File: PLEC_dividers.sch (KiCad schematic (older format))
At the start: 24 parts

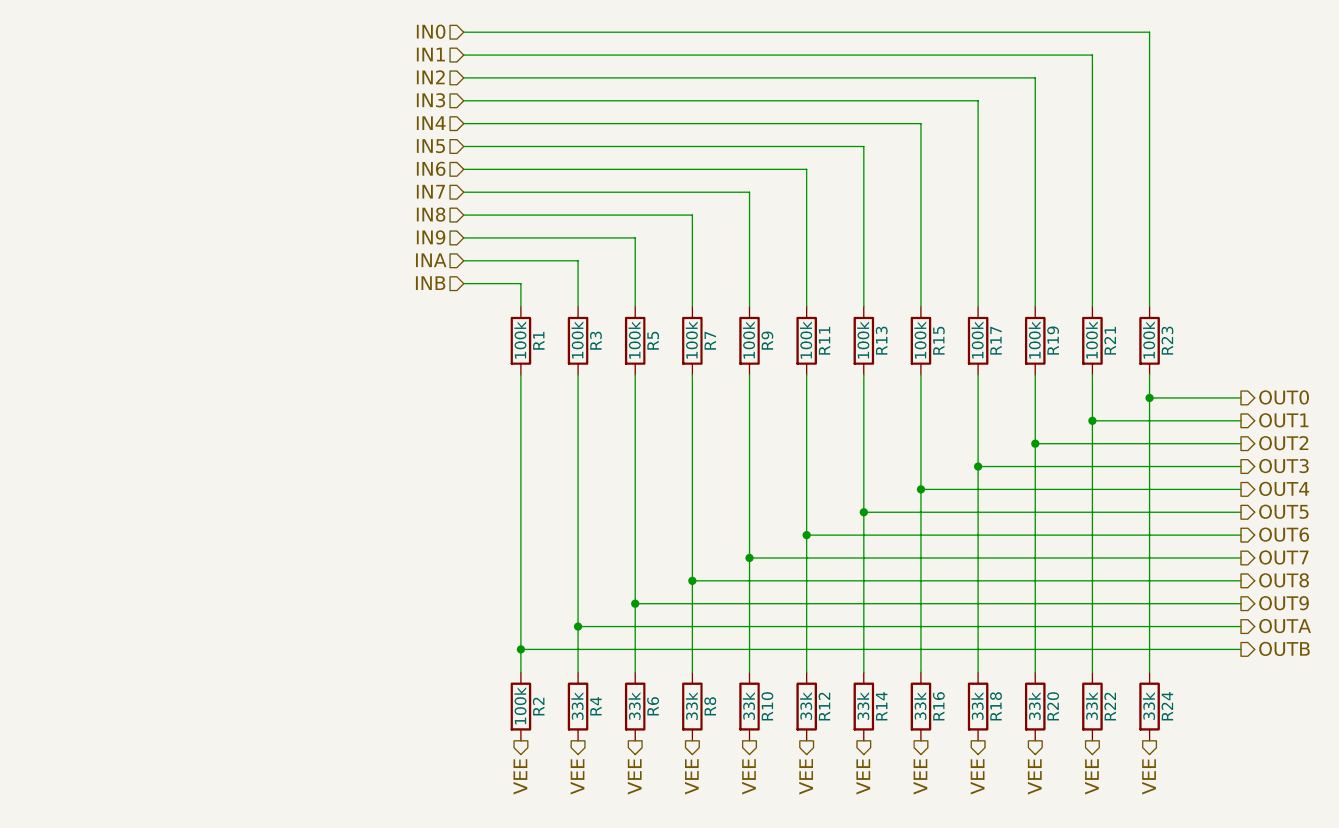
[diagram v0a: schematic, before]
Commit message: Replaced solid state relays with NPN Darlingtons
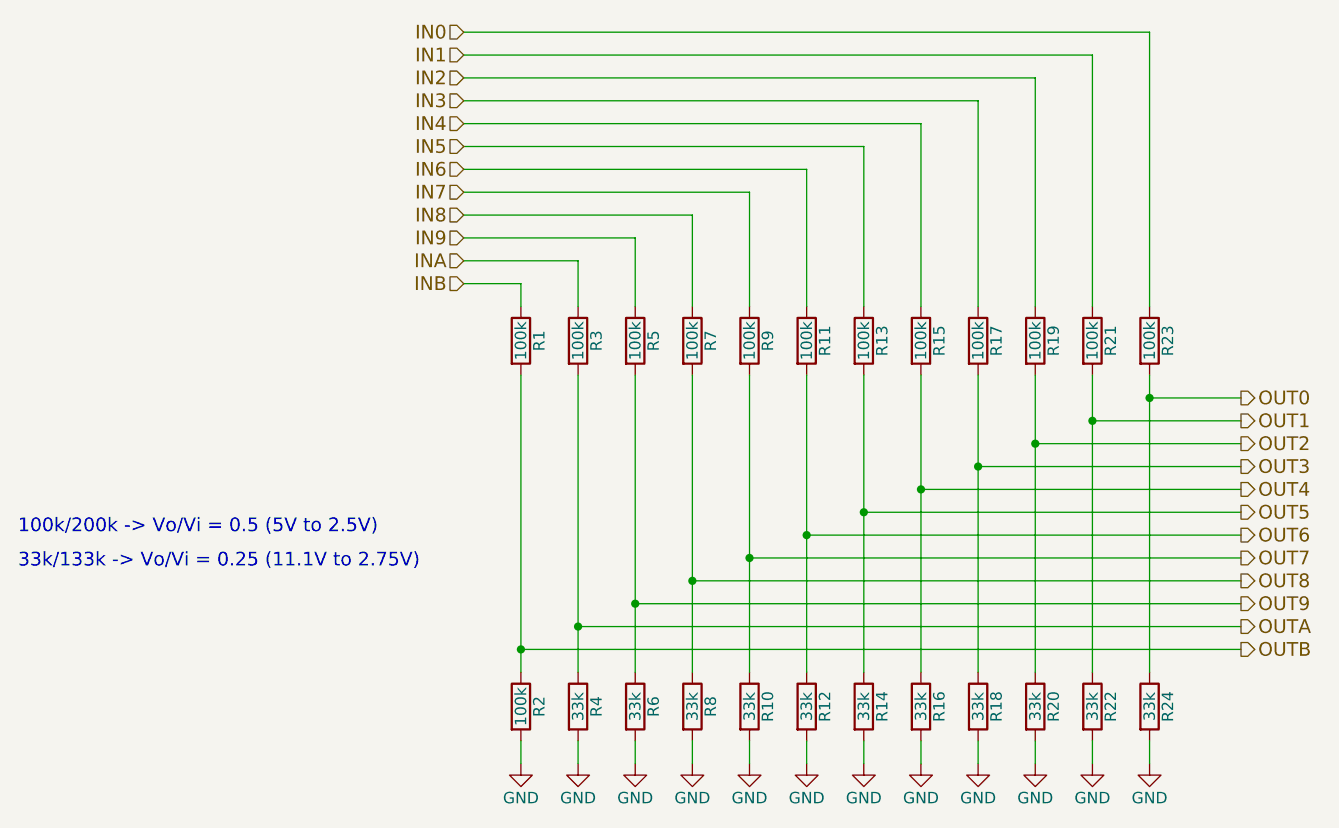
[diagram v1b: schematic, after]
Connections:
- net VEE renamed GND
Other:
- note added: "100k/200k -> Vo/Vi = 0.5 (5V to 2.5V)"
- note added: "33k/133k -> Vo/Vi = 0.25 (11.1V to 2.75V)"
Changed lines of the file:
@@
 EESchema Schematic File Version 2
+LIBS:PLEC-rescue
 LIBS:power
 LIBS:device
@@
 LIBS:PLEC
 LIBS:cap_470u
+LIBS:BDW42G
 LIBS:PLEC-cache
 EELAYER 25 0
@@
 Text HLabel 7400 4300 2    60   Output ~ 0
 OUT9
-Text HLabel 4750 4900 3    60   Output ~ 0
-VEE
-Text HLabel 5000 4900 3    60   Output ~ 0
-VEE
-Text HLabel 5250 4900 3    60   Output ~ 0
-VEE
-Text HLabel 5500 4900 3    60   Output ~ 0
-VEE
-Text HLabel 5750 4900 3    60   Output ~ 0
-VEE
-Text HLabel 6000 4900 3    60   Output ~ 0
-VEE
-Text HLabel 6250 4900 3    60   Output ~ 0
-VEE
-Text HLabel 6500 4900 3    60   Output ~ 0
-VEE
-Text HLabel 6750 4900 3    60   Output ~ 0
-VEE
-Text HLabel 7000 4900 3    60   Output ~ 0
-VEE
 $Comp
 L R R3
@@
 Text HLabel 4000 2800 0    60   Input ~ 0
 INA
-Text HLabel 4500 4900 3    60   Output ~ 0
-VEE
 Wire Wire Line
 	7400 4300 4750 4300
@@
 	1    0    0    -1
 $EndComp
-Text HLabel 4250 4900 3    60   Output ~ 0
-VEE
 Wire Wire Line
 	4250 3300 4250 4600
@@
 Text HLabel 7400 4500 2    60   Output ~ 0
 OUTB
+$Comp
+L GND #PWR05
+U 1 1 5A849DDD
+P 4500 5000
+F 0 "#PWR05" H 4500 4750 50  0001 C CNN
+F 1 "GND" H 4500 4850 50  0000 C CNN
+F 2 "" H 4500 5000 50  0001 C CNN
+F 3 "" H 4500 5000 50  0001 C CNN
+	1    4500 5000
+	1    0    0    -1
+$EndComp
+Wire Wire Line
+	4500 5000 4500 4900
+$Comp
+L GND #PWR06
+U 1 1 5A849F39
+P 4250 5000
+F 0 "#PWR06" H 4250 4750 50  0001 C CNN
+F 1 "GND" H 4250 4850 50  0000 C CNN
+F 2 "" H 4250 5000 50  0001 C CNN
+F 3 "" H 4250 5000 50  0001 C CNN
+	1    4250 5000
+	1    0    0    -1
+$EndComp
+Wire Wire Line
+	4250 5000 4250 4900
+$Comp
+L GND #PWR07
+U 1 1 5A849FC4
+P 4750 5000
+F 0 "#PWR07" H 4750 4750 50  0001 C CNN
+F 1 "GND" H 4750 4850 50  0000 C CNN
+F 2 "" H 4750 5000 50  0001 C CNN
+F 3 "" H 4750 5000 50  0001 C CNN
+	1    4750 5000
+	1    0    0    -1
+$EndComp
+Wire Wire Line
+	4750 5000 4750 4900
+$Comp
+L GND #PWR08
+U 1 1 5A849FE5
+P 5000 5000
+F 0 "#PWR08" H 5000 4750 50  0001 C CNN
+F 1 "GND" H 5000 4850 50  0000 C CNN
+F 2 "" H 5000 5000 50  0001 C CNN
+F 3 "" H 5000 5000 50  0001 C CNN
+	1    5000 5000
+	1    0    0    -1
+$EndComp
+Wire Wire Line
+	5000 5000 5000 4900
+$Comp
+L GND #PWR09
+U 1 1 5A84A6AE
+P 5250 5000
+F 0 "#PWR09" H 5250 4750 50  0001 C CNN
+F 1 "GND" H 5250 4850 50  0000 C CNN
+F 2 "" H 5250 5000 50  0001 C CNN
+F 3 "" H 5250 5000 50  0001 C CNN
+	1    5250 5000
+	1    0    0    -1
+$EndComp
+Wire Wire Line
+	5250 5000 5250 4900
+$Comp
+L GND #PWR010
+U 1 1 5A84A6CF
+P 5500 5000
+F 0 "#PWR010" H 5500 4750 50  0001 C CNN
+F 1 "GND" H 5500 4850 50  0000 C CNN
+F 2 "" H 5500 5000 50  0001 C CNN
+F 3 "" H 5500 5000 50  0001 C CNN
+	1    5500 5000
+	1    0    0    -1
+$EndComp
+Wire Wire Line
+	5500 5000 5500 4900
+$Comp
+L GND #PWR011
+U 1 1 5A84A6F0
+P 5750 5000
+F 0 "#PWR011" H 5750 4750 50  0001 C CNN
+F 1 "GND" H 5750 4850 50  0000 C CNN
+F 2 "" H 5750 5000 50  0001 C CNN
+F 3 "" H 5750 5000 50  0001 C CNN
+	1    5750 5000
+	1    0    0    -1
+$EndComp
+Wire Wire Line
+	5750 5000 5750 4900
+$Comp
+L GND #PWR012
+U 1 1 5A84A741
+P 6000 5000
+F 0 "#PWR012" H 6000 4750 50  0001 C CNN
+F 1 "GND" H 6000 4850 50  0000 C CNN
+F 2 "" H 6000 5000 50  0001 C CNN
+F 3 "" H 6000 5000 50  0001 C CNN
+	1    6000 5000
+	1    0    0    -1
+$EndComp
+Wire Wire Line
+	6000 5000 6000 4900
+$Comp
+L GND #PWR013
+U 1 1 5A84A762
+P 6250 5000
+F 0 "#PWR013" H 6250 4750 50  0001 C CNN
+F 1 "GND" H 6250 4850 50  0000 C CNN
+F 2 "" H 6250 5000 50  0001 C CNN
+F 3 "" H 6250 5000 50  0001 C CNN
+	1    6250 5000
+	1    0    0    -1
+$EndComp
+Wire Wire Line
+	6250 5000 6250 4900
+$Comp
+L GND #PWR014
+U 1 1 5A84A783
+P 6500 5000
+F 0 "#PWR014" H 6500 4750 50  0001 C CNN
+F 1 "GND" H 6500 4850 50  0000 C CNN
+F 2 "" H 6500 5000 50  0001 C CNN
+F 3 "" H 6500 5000 50  0001 C CNN
+	1    6500 5000
+	1    0    0    -1
+$EndComp
+Wire Wire Line
+	6500 5000 6500 4900
+$Comp
+L GND #PWR015
+U 1 1 5A84A7A4
+P 6750 5000
+F 0 "#PWR015" H 6750 4750 50  0001 C CNN
+F 1 "GND" H 6750 4850 50  0000 C CNN
+F 2 "" H 6750 5000 50  0001 C CNN
+F 3 "" H 6750 5000 50  0001 C CNN
+	1    6750 5000
+	1    0    0    -1
+$EndComp
+Wire Wire Line
+	6750 5000 6750 4900
+$Comp
+L GND #PWR016
+U 1 1 5A84A7C5
+P 7000 5000
+F 0 "#PWR016" H 7000 4750 50  0001 C CNN
+F 1 "GND" H 7000 4850 50  0000 C CNN
+F 2 "" H 7000 5000 50  0001 C CNN
+F 3 "" H 7000 5000 50  0001 C CNN
+	1    7000 5000
+	1    0    0    -1
+$EndComp
+Wire Wire Line
+	7000 5000 7000 4900
+Text Notes 2050 4000 0    60   ~ 0
+100k/200k -> Vo/Vi = 0.5 (5V to 2.5V)
+Text Notes 2050 4150 0    60   ~ 0
+33k/133k -> Vo/Vi = 0.25 (11.1V to 2.75V)
 $EndSCHEMATC
